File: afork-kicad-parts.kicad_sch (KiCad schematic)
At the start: 34 parts, among them J1 CAN_BUS, J2 Raspberry_Pi, J3 USB_A, J4 USB_C_Receptacle_USB2.0_14P, M1 Arduino_Mini, M2 DCDC_CONVERTER_CCCV_ADJ, M3 Motor_AC, M4 TINYPICO, P1 Conn_WallPlug_Earth, P2 DC_CONN, T1 Tooling, U1 24LC32, U10 RCLAMP0524P-N, U11 SRV05-4, U12 SSD1306_OLED_128x64, U13 TCAN332, U2 ATMEGA168A-AU, U3 ESP32-S3-WROOM-1, U4 LMR38020, U6 M24C64, U7 MP2451, U8 NE555P, U9 OLED128X64, X1 MHz

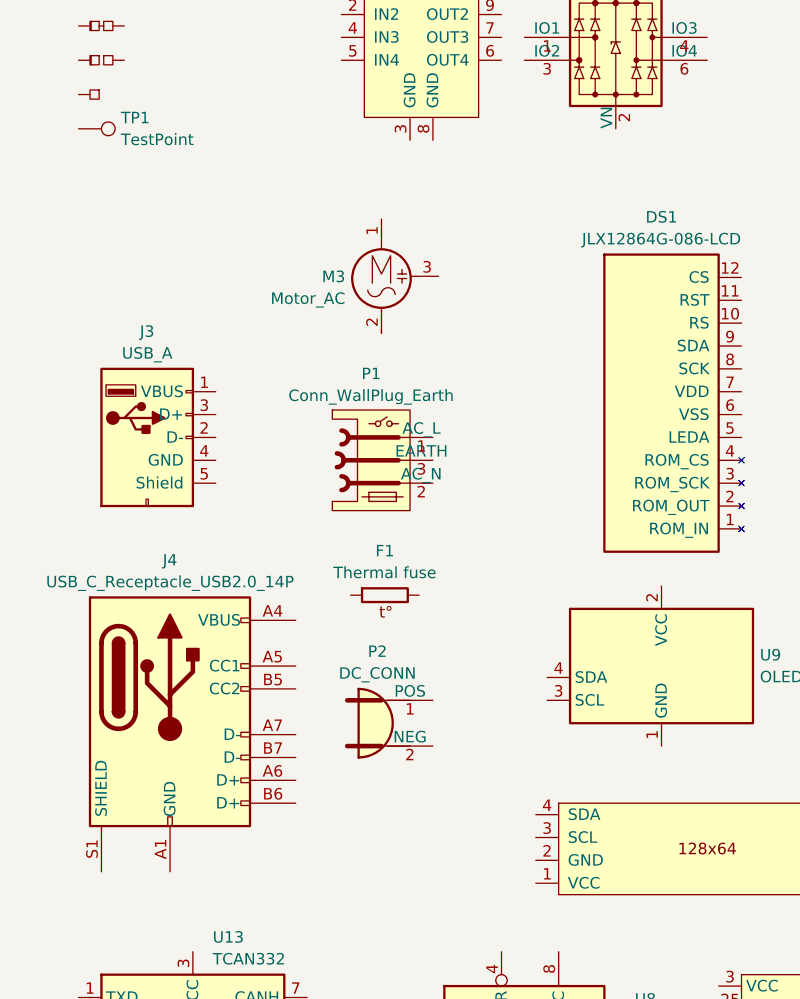
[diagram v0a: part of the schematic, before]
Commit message: Put Tinker's USB Type-C socket on board.
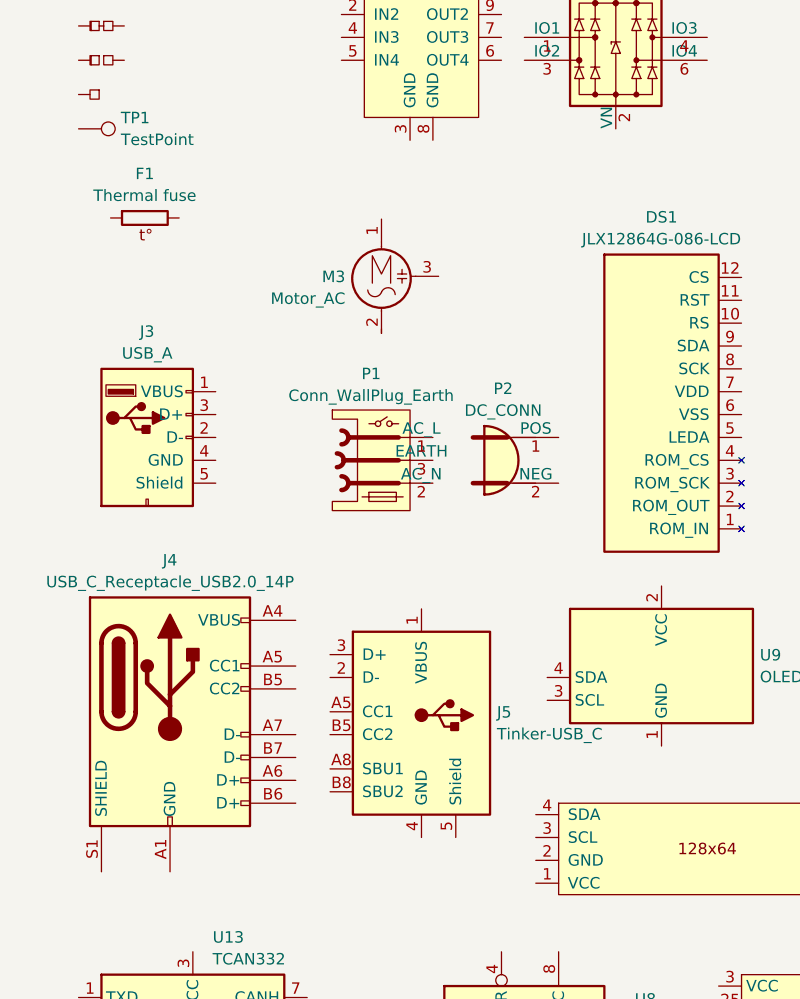
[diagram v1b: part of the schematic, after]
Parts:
- added J5: Tinker-USB_C, afork-kicad-parts:Tinker-USB_C, symbol afork-kicad-parts:Tinker-USB_C
- U3: footprint Espressif:ESP32-S3-WROOM-1 -> RF_Module:ESP32-S3-WROOM-1
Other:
- moved on the sheet: F1, P2
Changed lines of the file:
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@@
 			)
 		)
-		(property "Footprint" "Espressif:ESP32-S3-WROOM-1"
+		(property "Footprint" "RF_Module:ESP32-S3-WROOM-1"
 			(at 234.95 123.19 0)
 			(effects
@@
 	(symbol
 		(lib_id "afork-kicad-parts:DC_CONN")
-		(at 49.53 107.95 0)
+		(at 63.5 78.74 0)
 		(unit 1)
 		(exclude_from_sim no)
@@
 		(fields_autoplaced yes)
 		(property "Reference" "P2"
-			(at 48.4505 99.9955 0)
+			(at 62.4205 70.7855 0)
 			(effects
 				(font
@@
 		)
 		(property "Value" "DC_CONN"
-			(at 48.4505 102.4198 0)
+			(at 62.4205 73.2098 0)
 			(effects
 				(font
@@
 		)
 		(property "Footprint" ""
-			(at 59.69 107.95 0)
+			(at 73.66 78.74 0)
 			(effects
 				(font
@@
 		)
 		(property "Datasheet" ""
-			(at 59.69 107.95 0)
+			(at 73.66 78.74 0)
 			(effects
 				(font
@@
 		)
 		(property "Description" ""
-			(at 49.53 107.95 0)
+			(at 63.5 78.74 0)
 			(effects
 				(font
@@
 	)
 	(symbol
+		(lib_id "afork-kicad-parts:Tinker-USB_C")
+		(at 53.34 107.95 0)
+		(unit 1)
+		(exclude_from_sim no)
+		(in_bom yes)
+		(on_board yes)
+		(dnp no)
+		(fields_autoplaced yes)
+		(property "Reference" "J5"
+			(at 61.722 106.7378 0)
+			(effects
+				(font
+					(size 1.27 1.27)
+				)
+				(justify left)
+			)
+		)
+		(property "Value" "Tinker-USB_C"
+			(at 61.722 109.1621 0)
+			(effects
+				(font
+					(size 1.27 1.27)
+				)
+				(justify left)
+			)
+		)
+		(property "Footprint" "afork-kicad-parts:Tinker-USB_C"
+			(at 53.34 134.62 0)
+			(effects
+				(font
+					(size 1.27 1.27)
+				)
+				(hide yes)
+			)
+		)
+		(property "Datasheet" " ~"
+			(at 57.15 109.22 0)
+			(effects
+				(font
+					(size 1.27 1.27)
+				)
+				(hide yes)
+			)
+		)
+		(property "Description" "USB Type C connector"
+			(at 53.34 107.95 0)
+			(effects
+				(font
+					(size 1.27 1.27)
+				)
+				(hide yes)
+			)
+		)
+		(property "LCSC" "C2765186"
+			(at 63.5 107.95 90)
+			(effects
+				(font
+					(size 1.27 1.27)
+				)
+				(hide yes)
+			)
+		)
+		(pin "B5"
+		)
+		(pin "A5"
+		)
+		(pin "1"
+		)
+		(pin "4"
+		)
+		(pin "3"
+		)
+		(pin "2"
+		)
+		(pin "B8"
+		)
+		(pin "A8"
+		)
+		(pin "5"
+		)
+		(instances
+			(project "afork-kicad-parts"
+				(path "/cb8f6e0d-a02c-4a1b-9ae5-b293992d3fe7"
+					(reference "J5")
+					(unit 1)
+				)
+			)
+		)
+	)
+	(symbol
 		(lib_id "afork-kicad-parts:JLX12864G-086-LCD")
 		(at 80.01 72.39 0)
@@
 	(symbol
 		(lib_id "afork-kicad-parts:Thermal fuse")
-		(at 49.149 93.599 0)
+		(at 22.479 51.689 0)
 		(unit 1)
 		(exclude_from_sim no)
@@
 		(fields_autoplaced yes)
 		(property "Reference" "F1"
-			(at 49.276 88.8195 0)
+			(at 22.606 46.9095 0)
 			(effects
 				(font
@@
 		)
 		(property "Value" "Thermal fuse"
-			(at 49.276 91.2438 0)
+			(at 22.606 49.3338 0)
 			(effects
 				(font
@@
 		)
 		(property "Footprint" ""
-			(at 49.276 95.504 0)
+			(at 22.606 53.594 0)
 			(effects
 				(font
@@
 		)
 		(property "Datasheet" "~"
-			(at 49.276 93.726 0)
+			(at 22.606 51.816 0)
 			(effects
 				(font
@@
 		)
 		(property "Description" "Fuse"
-			(at 49.276 93.726 0)
-			(effects
-				(font
+			(at 22.606 51.816 0)
+			(effects
+				(font

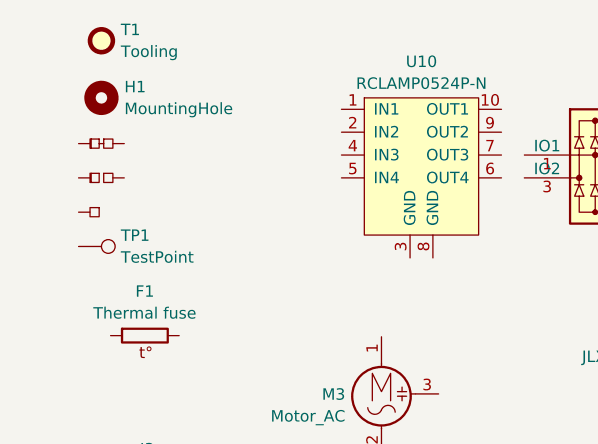
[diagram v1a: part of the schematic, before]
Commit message: Clean up jumpers to allow mine and Tinker's.
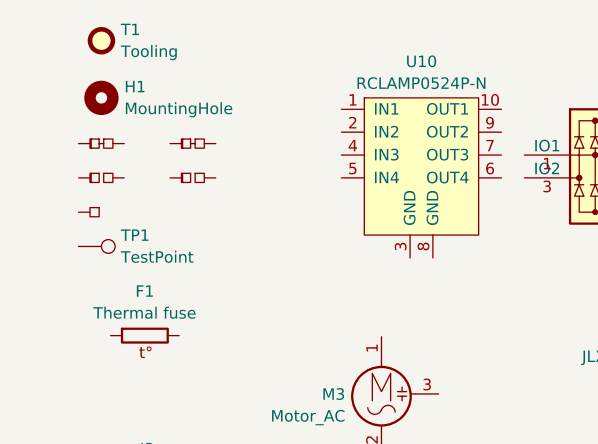
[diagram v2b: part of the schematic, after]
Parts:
- added JP4: PCB_Patch, afork-kicad-parts:tinySJ-Bridged, symbol afork-kicad-parts:PCB_Patch
- added JP5: PCB_Patch-open, afork-kicad-parts:tinySJ-Open, symbol afork-kicad-parts:PCB_Patch-open
- JP1: footprint ozhelm:SolderJumper-2_P1.3mm_Bridged_Pad1.0x1.5mm -> afork-kicad-parts:SolderJumper-2_P1.3mm_Bridged_Pad1.0x1.5mm
- JP2: footprint ozhelm:SolderJumper-2_P1.3mm_Open_Pad1.0x1.5mm -> afork-kicad-parts:SolderJumper-2_P1.3mm_Open_Pad1.0x1.5mm
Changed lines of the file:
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@@
 			)
 		)
-		(property "Footprint" "ozhelm:SolderJumper-2_P1.3mm_Open_Pad1.0x1.5mm"
+		(property "Footprint" "afork-kicad-parts:SolderJumper-2_P1.3mm_Open_Pad1.0x1.5mm"
 			(at 17.78 34.29 0)
 			(effects
@@
 			)
 		)
-		(property "Footprint" "ozhelm:SolderJumper-2_P1.3mm_Bridged_Pad1.0x1.5mm"
+		(property "Footprint" "afork-kicad-parts:SolderJumper-2_P1.3mm_Bridged_Pad1.0x1.5mm"
 			(at 19.05 26.67 0)
 			(effects
@@
 	)
 	(symbol
+		(lib_id "afork-kicad-parts:PCB_Patch-open")
+		(at 27.94 34.29 0)
+		(unit 1)
+		(exclude_from_sim no)
+		(in_bom no)
+		(on_board yes)
+		(dnp no)
+		(fields_autoplaced yes)
+		(property "Reference" "JP5"
+			(at 27.94 32.258 0)
+			(effects
+				(font
+					(size 1.27 1.27)
+				)
+				(hide yes)
+			)
+		)
+		(property "Value" "PCB_Patch-open"
+			(at 28.194 35.814 0)
+			(effects
+				(font
+					(size 1.27 1.27)
+				)
+				(hide yes)
+			)
+		)
+		(property "Footprint" "afork-kicad-parts:tinySJ-Open"
+			(at 27.94 34.29 0)
+			(effects
+				(font
+					(size 1.27 1.27)
+				)
+				(hide yes)
+			)
+		)
+		(property "Datasheet" "~"
+			(at 27.94 34.29 0)
+			(effects
+				(font
+					(size 1.27 1.27)
+				)
+				(hide yes)
+			)
+		)
+		(property "Description" "Jumper, normally open, small symbol"
+			(at 27.94 34.29 0)
+			(effects
+				(font
+					(size 1.27 1.27)
+				)
+				(hide yes)
+			)
+		)
+		(pin "2"
+		)
+		(pin "1"
+		)
+		(instances
+			(project "afork-kicad-parts"
+				(path "/cb8f6e0d-a02c-4a1b-9ae5-b293992d3fe7"
+					(reference "JP5")
+					(unit 1)
+				)
+			)
+		)
+	)
+	(symbol
 		(lib_id "afork-kicad-parts:SSD1306_OLED_128x64")
 		(at 81.28 123.19 0)
@@
 					(unit 1)
 				)
+			)
+		)
+	)
+	(symbol
+		(lib_id "afork-kicad-parts:PCB_Patch")
+		(at 27.94 30.48 0)
+		(unit 1)
+		(exclude_from_sim no)
+		(in_bom no)
+		(on_board yes)
+		(dnp no)
+		(fields_autoplaced yes)
+		(property "Reference" "JP4"
+			(at 27.94 28.448 0)
+			(effects
+				(font
+					(size 1.27 1.27)
+				)
+				(hide yes)
+			)
+		)
+		(property "Value" "PCB_Patch"
+			(at 28.194 32.004 0)
+			(effects
+				(font
+					(size 1.27 1.27)
+				)
+				(hide yes)
+			)
+		)
+		(property "Footprint" "afork-kicad-parts:tinySJ-Bridged"
+			(at 29.21 26.67 0)
+			(effects
+				(font
+					(size 1.27 1.27)
+				)
+				(hide yes)
+			)
+		)
+		(property "Datasheet" "~"
+			(at 27.94 30.48 0)
+			(effects
+				(font
+					(size 1.27 1.27)
+				)
+				(hide yes)
+			)
+		)
+		(property "Description" "Jumper, normally closed, small symbol"
+			(at 27.94 30.48 0)
+			(effects
+				(font
+					(size 1.27 1.27)
+				)
+				(hide yes)
+			)
+		)
+		(pin "2"
+		)
+		(pin "1"
+		)
+		(instances
+			(project "afork-kicad-parts"
+				(path "/cb8f6e0d-a02c-4a1b-9ae5-b293992d3fe7"
+					(reference "JP4")
+					(unit 1)
+				)
